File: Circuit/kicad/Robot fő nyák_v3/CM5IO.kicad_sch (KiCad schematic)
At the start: 1 part, among them SW3 SW_DIP_x05

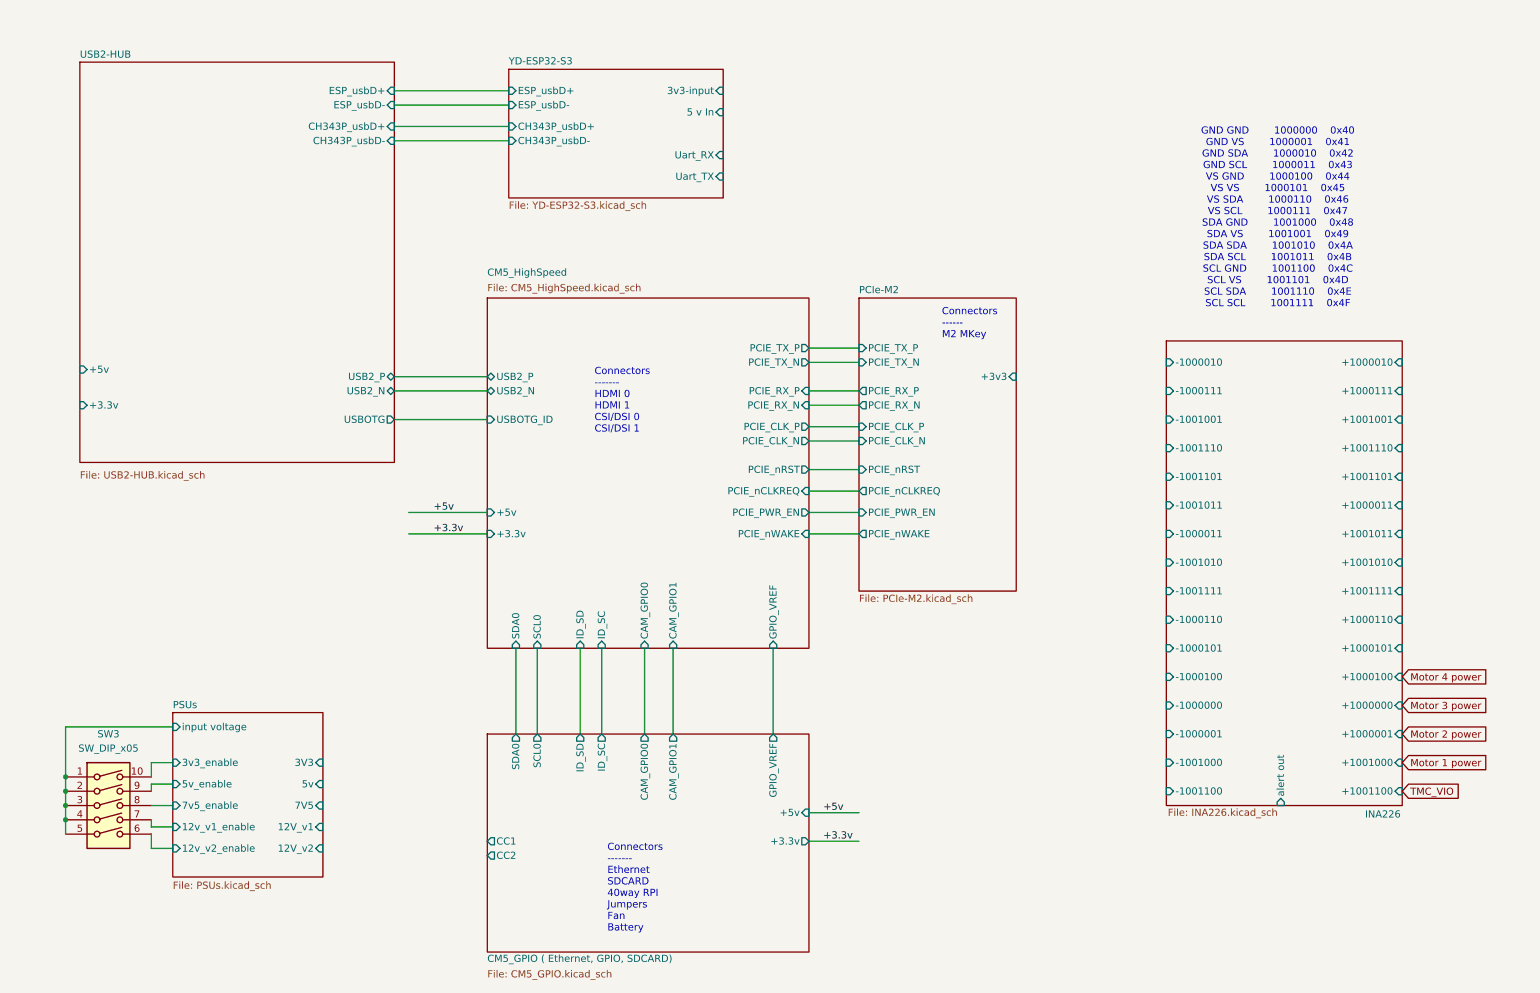
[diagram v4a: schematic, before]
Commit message: Kicad update: power rails v1.0, todo: hc-sr-04  as6500 ic review shift registers change to MCP23S17_SO
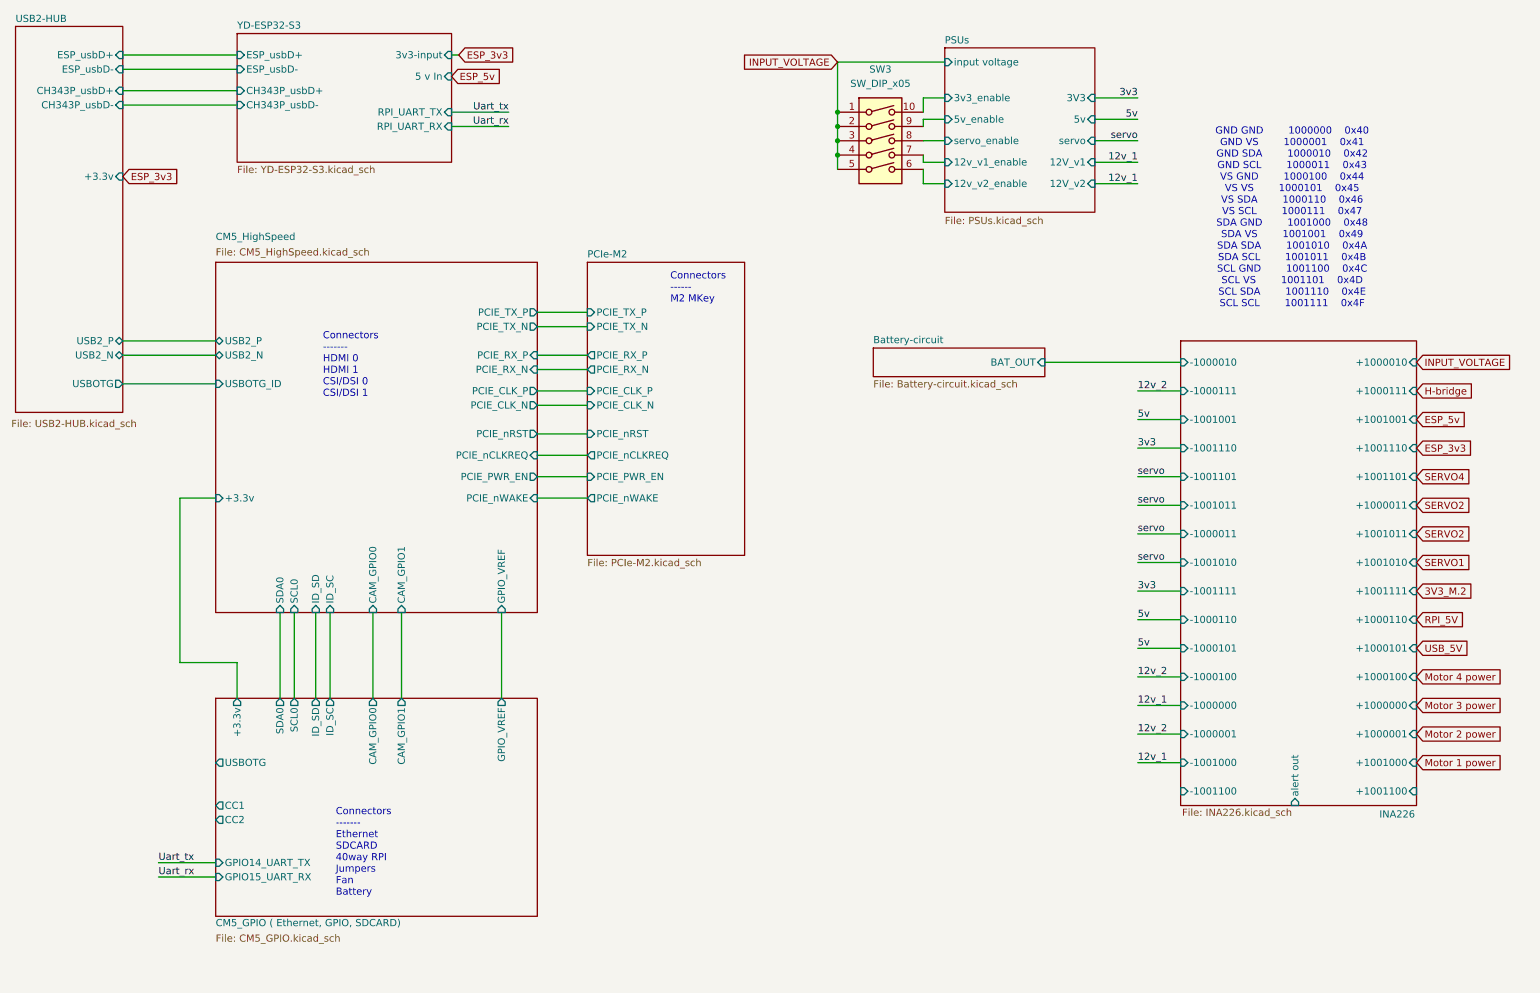
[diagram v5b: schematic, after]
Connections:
- net PSUs/7v5_enable renamed PSUs/servo_enable
- net PSUs/input voltage renamed INPUT_VOLTAGE
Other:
- added sheet Battery-circuit (Battery-circuit.kicad_sch)
- sheet CM5_GPIO ( Ethernet, GPIO, SDCARD) ports: added GPIO14_UART_TX, GPIO15_UART_RX, USBOTG; removed +5v
- sheet CM5_HighSpeed ports: added none; removed +5v
- sheet PCIe-M2 ports: added none; removed +3v3
- sheet PSUs ports: added servo, servo_enable; removed 7V5, 7v5_enable
- sheet USB2-HUB ports: added none; removed +5v
- sheet YD-ESP32-S3 ports: added RPI_UART_RX, RPI_UART_TX; removed Uart_RX, Uart_TX
- moved on the sheet: SW3

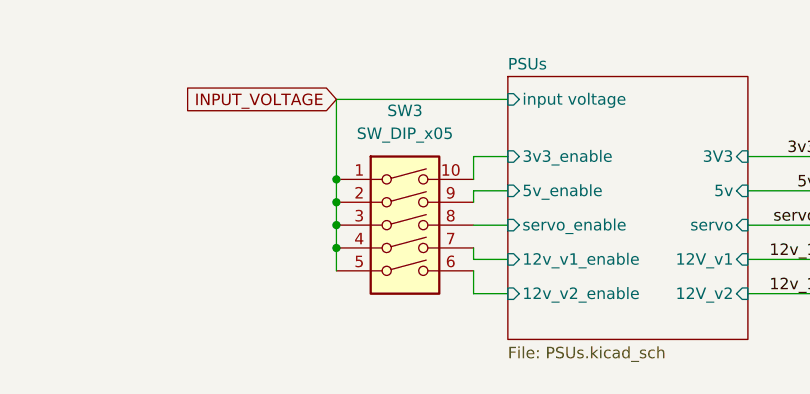
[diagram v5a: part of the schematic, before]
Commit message: kicad v0.1 footprint- assing spi finish
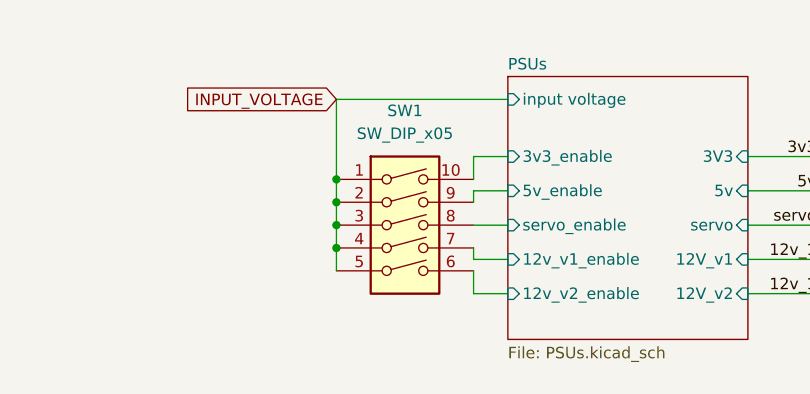
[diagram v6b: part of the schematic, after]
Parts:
- SW1: renamed from SW3; footprint (none) -> Resistor_SMD:R_0805_2012Metric
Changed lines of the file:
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@@
 		(dnp no)
 		(fields_autoplaced yes)
-		(property "Reference" "SW3"
+		(property "Reference" "SW1"
 			(at 171.45 24.13 0)
 			(effects
@@
 			)
 		)
-		(property "Footprint" ""
+		(property "Footprint" "Resistor_SMD:R_0805_2012Metric"
 			(at 171.45 36.83 0)
 			(effects
@@
 			(project ""
 				(path "/e63e39d7-6ac0-4ffd-8aa3-1841a4541b55"
-					(reference "SW3")
+					(reference "SW1")
 					(unit 1)
 				)

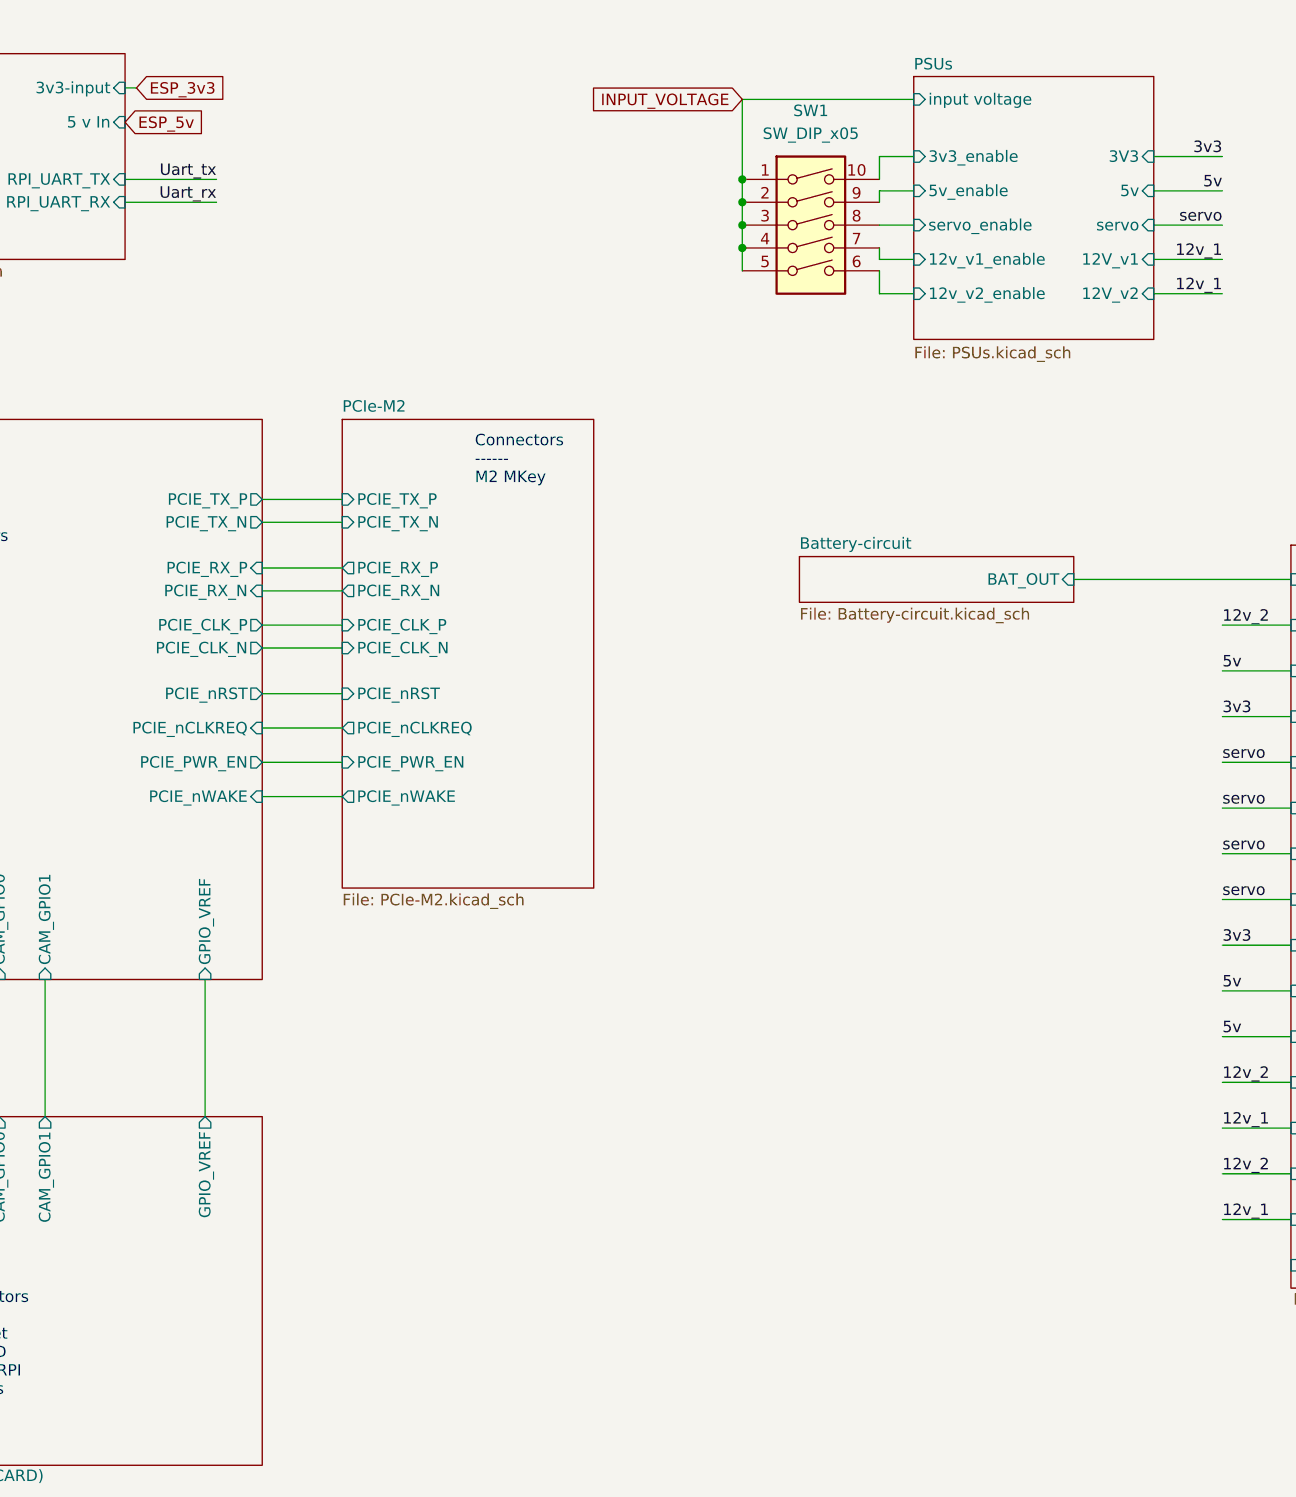
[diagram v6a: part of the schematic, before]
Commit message: kicad  i2c and spi mux fixed and bugfixs
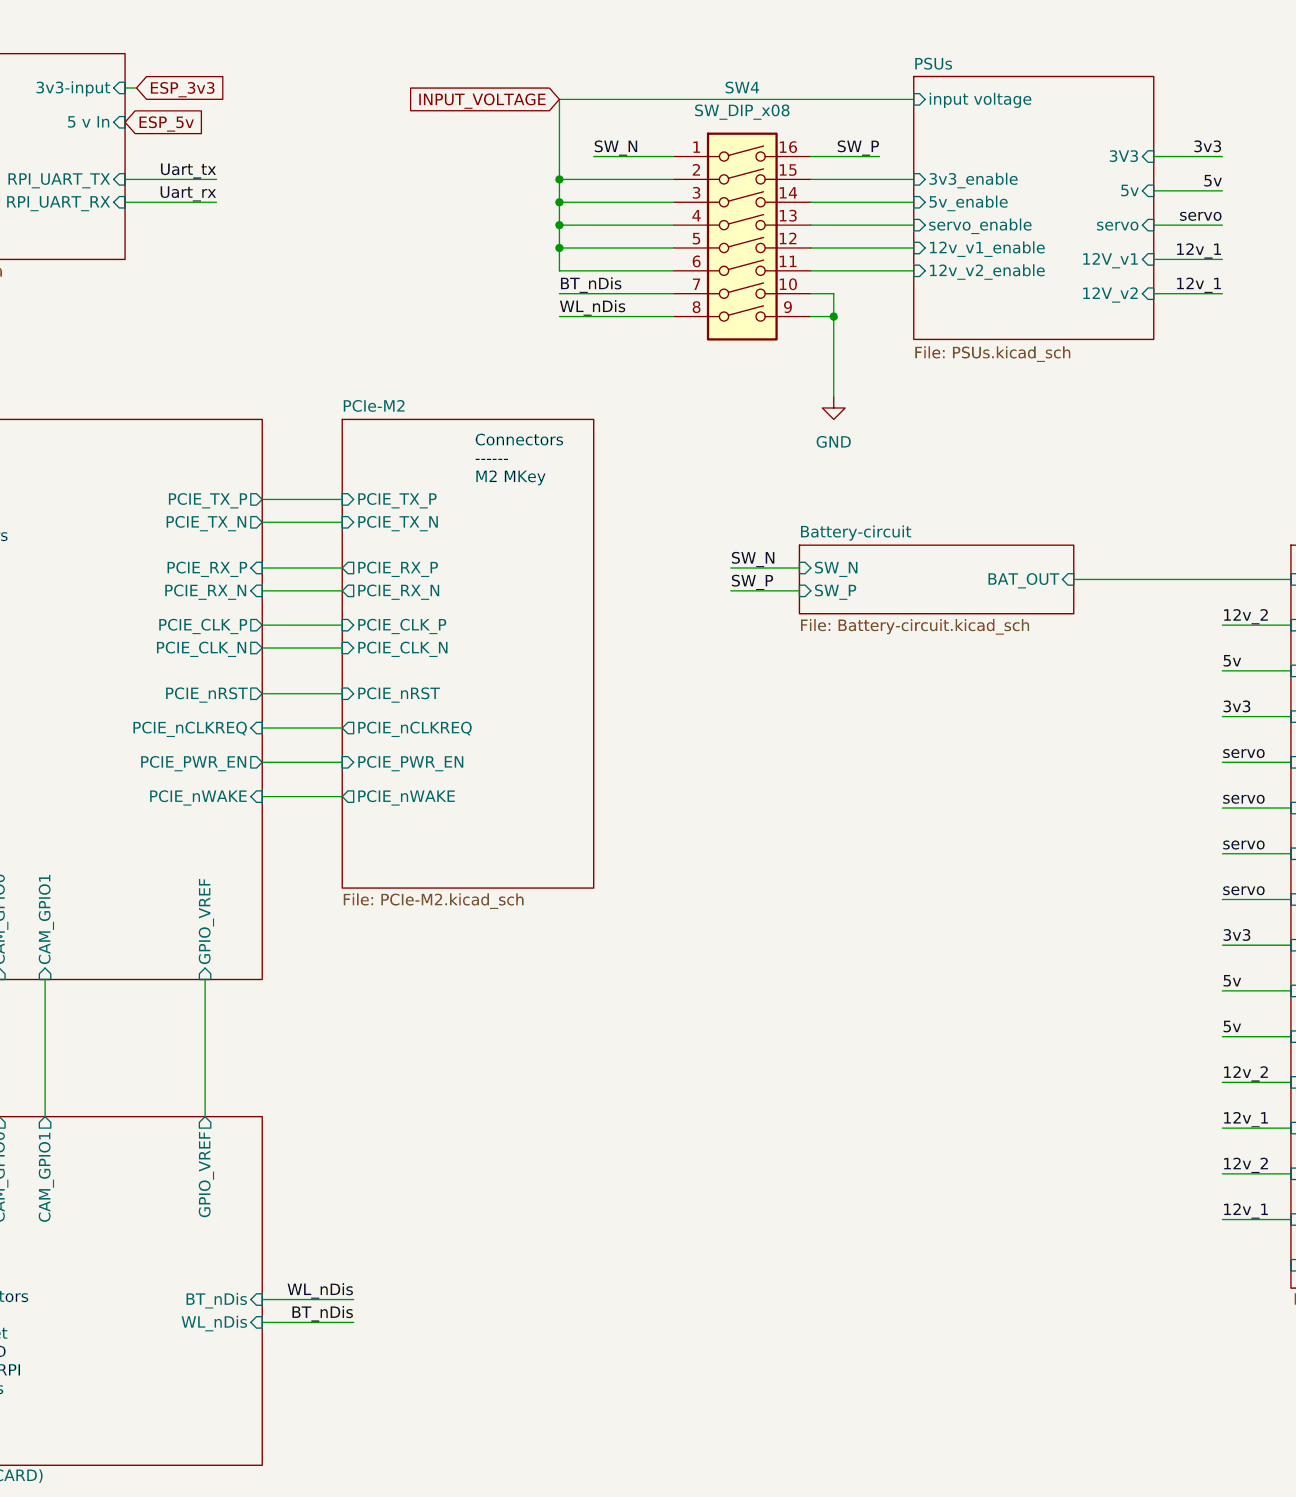
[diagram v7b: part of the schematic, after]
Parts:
- removed SW1: SW_DIP_x05, Resistor_SMD:R_0805_2012Metric, symbol Switch:SW_DIP_x05
- added SW4: SW_DIP_x08, Button_Switch_SMD:SW_DIP_SPSTx08_Slide_Copal_CHS-08A_W5.08mm_P1.27mm_JPin, symbol Switch:SW_DIP_x08
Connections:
- net INPUT_VOLTAGE: now also SW4.2, SW4.3, SW4.4, SW4.5, SW4.6
- net PSUs/12v_v1_enable: now also SW4.12
- net PSUs/12v_v2_enable: now also SW4.11
- net PSUs/3v3_enable: now also SW4.15
- net PSUs/5v_enable: now also SW4.14
- net PSUs/servo_enable: now also SW4.13
- new net BT_nDis: SW4.7
- new net GND: SW4.10, SW4.9
- new net SW_N: SW4.1
- new net SW_P: SW4.16
- new net WL_nDis: SW4.8
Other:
- sheet Battery-circuit ports: added SW_N, SW_P; removed none
- sheet CM5_GPIO ( Ethernet, GPIO, SDCARD) ports: added BT_nDis, WL_nDis; removed none
